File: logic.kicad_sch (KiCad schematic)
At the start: 15 parts, among them U1 SN74ALS08 (КР1533ЛИ1), U11 IN74ALS00N (КР1533ЛА3), U12 IN74ALS02N (КР1533ЛЕ1), U13 SN74ALS10 (КР1533ЛА4), U15 CD4520АN_(К561ИЕ10), U19 SN74ALS04 (КР1533ЛН1), U2 SN74ALS04 (КР1533ЛН1), U3 SN74ALS74AN (КР1533ТМ2), U4 SN74ALS193N_(КР1533ИЕ7), Y1 14 MHz

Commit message: March 21st update
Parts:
- added C3: 220pF, symbol Device:C
- added C32: 82pF, symbol Device:C
- added C8: 120pF, symbol Device:C
- added R15: 510, symbol Device:R
- added R19: 180, symbol Device:R
- added R4, R8: 160, symbol Device:R
- added R5: 10K, symbol Device:R
- added U10: SN74ALS08 (КР1533ЛИ1), Package_DIP:DIP-14_W7.62mm_Socket_LongPads, symbol 74xx:74LS08
- added U14: SN74ALS86N (КР1533ЛП5), Package_DIP:DIP-14_W7.62mm_Socket_LongPads, symbol 74xx:74LS86
- added U17: CD4520АN_(К561ИЕ10), Package_DIP:DIP-16_W7.62mm_Socket_LongPads, symbol w_connectors:CD4520АN_(К561ИЕ10)
- added U18: CD4011 (К561ЛА7), Package_DIP:DIP-14_W7.62mm_Socket_LongPads, symbol 4xx:4011
- added unit 5 of U19
- added unit 3 of U19
- added U20: SN74ALS74AN (КР1533ТМ2), Package_DIP:DIP-14_W7.62mm_Socket_LongPads, symbol 74xx:74LS74
- added U28: IN74ALS32N (КР1533ЛЛ1), Package_DIP:DIP-14_W7.62mm_Socket_LongPads, symbol 74xx:74LS32
- added U49, U7: SN74ALS04 (КР1533ЛН1), Package_DIP:DIP-14_W7.62mm_Socket_LongPads, symbol 74xx:74LS04
- added U5: СD4013АN_(К561ТМ2), Package_DIP:DIP-14_W7.62mm_Socket_LongPads, symbol w_connectors:СD4013АN_(К561ТМ2)
- added U6: CD4015A (К561ИР2), Package_DIP:DIP-16_W7.62mm_Socket_LongPads, symbol 4xxx_IEEE:4015
- added U8, U9: СD4001АN (К561ЛЕ5), Package_DIP:DIP-14_W7.62mm_Socket_LongPads, symbol 4xx:4001
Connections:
- net +5V: now also U15.10 (Enable), U3.10 (~{S}), U3.13 (~{R}), R15.2, U14.10, U20.1 (~{R}), U5.14 (Ucc), U6.16 (Vdd)
- net 7MHZ: now also U11.5, U3.11 (C)
- net GND: now also C3.1, C32.1, C8.1, U17.1 (CK), U17.9 (CK), U5.10 (R2), U5.6 (S1), U5.7 (GND), U5.8 (S2), U6.8 (Vss)
- net UPRMX: now also U19.11
- net at U11.10, U12.5, U4.3 (QA): now also U11.4, U19.5
- net at U11.8, U13.3, U2.1: now also U13.2
- net at U3.5 (Q), U4.5 (UP): now also U20.3 (C)
- net at U1.9, U13.5, U4.6 (QC): now also U14.5
- net at U11.11: now also U1.5
- net at U11.12: now also U11.6
- net ZPRGBD: now reaches U11.13
- net ZPRGBD: now also U3.8 (~{Q})
- net at U3.12 (D): now also U1.13, U13.12
- net BA1: now reaches U15.11 (Q1)
- net BA1: now also U5.11 (C2)
- net BA2: now reaches U15.12 (Q2)
- net BA2: now also R4.1, R5.1
- net BA3: now reaches U15.13 (Q3)
- net BA4: now reaches U15.14 (Q4)
- net BA4: now also U5.4 (R1), U6.7 (D)
- net at U15.15 (Reset): now also U6.6 (MR), U8.10
- net BA0: now reaches U13.4, U15.9 (CK), U4.7 (QD)
- net BA0: now also U14.4
- net at U13.6: now also U10.13
- net at U13.11: now also U13.13, U14.6
- net at U1.4: now also C32.2, R8.2
- net BCASL: now reaches U1.6
- net BRASL: now reaches U1.11
- net at U1.12: now also R8.1, U14.8
- net at U13.1: now also U10.12
- new net: C3.2, R4.2, U7.1
- new net: U18.8, U6.9 (CP), U7.2
- new net: U18.9, U5.1 (Q1), U5.9 (D2)
- new net: U19.10, U28.9
- new net: U10.11, U20.4 (~{S})
- new net: U10.2, U20.5 (Q)
- new net: U7.8, U8.8
- new net: U6.10 (Q4), U7.9, U8.6, U8.9
- new net: U10.3, U49.3
- new net: C8.2, R19.2, U14.9
- new net: R5.2, U5.3 (C1)
- new net: U10.1, U19.6
- new net: U5.5 (D1), U6.3 (Q3), U8.5
- new net: U18.2, U5.12 (Q2o)
- new net BA12: U28.8
- new net BA5: U17.14 (Q4), U17.2 (Enable)
- new net CCML: U17.10 (Enable), U18.10
- new net CT9: U28.10
- new net KGIL: U18.1
- new net KKADRAN: U17.15 (Reset), U17.7 (Reset)
- new net KSGIN: U18.3
- new net OZUMPN: R19.1
- new net VOZUL: U20.2 (D)
- new net Vdd: U6.16 (Vdd)
- new net Vss: U6.8 (Vss)
- new net ТАКТ: R15.1, U49.4
- no-connect marks 2 -> 8
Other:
- note removed: "u10"
- moved on the sheet: C1, C6, R1, R10, R2, U11C, U12B, U13A, U13B, U13C, U15B, U19B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

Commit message: March 22nd additions
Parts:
- added C7: X, symbol Device:C
- added R9, R?: X, symbol Device:R
- added unit 4 of U14
- added unit 6 of U19
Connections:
- net BA0: now also U20.11 (C)
- net BRASL: now also R9.1
- net GND: now also C7.1, U14.13
- net at U20.10 (~{S}): now also U20.13 (~{R})
- net at U20.12 (D): now also U10.12, U10.6, U13.1
- net at U20.9 (Q): now also R?.2
- net at U10.5: now also U8.4
- new net: R?.1, U19.13
- new net: C7.2, R9.2, U14.12
- new net BMX: U14.11
- new net KRAIN: U19.12
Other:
- moved on the sheet: U10B, U18B, U20B, U7B, U7C, U7E, U7F, U9A, U9B, U9C, U9D

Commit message: March 22nd update 2
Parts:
- added C12, C5: Х, symbol Device:C
- added R6: X, symbol Device:R
- added unit 4 of U19
- added U?: SN74ALS257N_(КР1533КП11А), Package_DIP:DIP-16_W7.62mm_Socket_LongPads, symbol w_connectors:SN74ALS257N_(КР1533КП11А)
- gave numbers to parts that had none: 1
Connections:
- net +5V: now also U?.16 (VCC)
- net BA5: now also U6.1 (CP), U9.9
- net CT9: now also U17.5 (Q3), U18.5, U?.13 (I1c), U?.5 (I0b)
- net GND: now also U?.8 (GND)
- net KGIL: now also U9.4
- net KKADRAN: now also U9.11, U19.9
- net UPRMX: now also U?.1 (S)
- net at U7.5: now also U7.4, U8.1, U8.13, U9.13
- net at U7.6: now also R6.2
- net at U7.12: now also U8.2
- net at U7.13: now also U18.4, U6.15 (D)
- net at R13.1, U19.13: now also C12.1
- net at U9.1: now also U6.2 (Q4), U7.3
- net at U9.2: now also U6.13 (Q1)
- net at U9.3: now also U9.5
- net BA6: now reaches U17.3 (Q1)
- net BA7: now reaches U17.4 (Q2)
- net at U17.6 (Q4): now also U18.6
- net at U9.10: now also U18.12, U9.6
- net at U9.8: now also U7.10
- net at U8.11: now also U7.11
- net at U8.12: now also U6.11 (Q3)
- net at U9.12: now also C5.2, R6.1
- net TAIMS: now reaches U18.11
- net CT4: now reaches U18.13
- net CT4: now also U17.13 (Q3), U?.10 (I1d)
- net at U6.14 (MR): now also C12.2, C5.1
- net at U17.11 (Q1): now also U?.6 (I1b)
- net at U17.12 (Q2): now also U?.3 (I1a)
- new net BA10: U?.9 (Zd)
- new net BA11: U?.12 (Zc)
- new net BA8: U?.7 (Zb)
- new net BA9: U?.4 (Za)
- new net ПРL: U19.8
- no-connect marks 8 -> 9
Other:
- moved on the sheet: C32, U10C, U10E, U11A, U11E, U13D, U17A, U17B, U17C, U18B, U18D, U18E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

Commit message: March 22nd - 3rd edition
List 3 is complete
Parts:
- removed C7: X, symbol Device:C
- added C4: 1000pF, symbol Device:C
- C12: value Х -> 120pF
- C5: value Х -> 1000pF
- R13, R9: value X -> 160
- R6: value X -> 10K
- gave numbers to parts that had none: 1
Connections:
- net Vdd is gone; now on net +5V: U6.16 (Vdd)
- net Vss is gone; now on net GND: U6.8 (Vss)
- net +5V: now also U1.14 (VCC), U10.14 (VCC), U11.14 (VCC), U13.14 (VCC), U17.16 (VDD), U18.14 (VDD), U2.14 (VCC), U20.14 (VCC), U28.14 (VCC), U3.14 (VCC), U7.14 (VCC), U8.14 (VDD), U9.14 (VDD)
- net GND: now also C12.2, C5.1, U1.7 (GND), U10.7 (GND), U11.7 (GND), U13.7 (GND), U16.11 (I0d), U16.15 (OE), U17.8 (VSS), U18.7 (VSS), U2.7 (GND), U20.7 (GND), U28.7 (GND), U3.7 (GND), U6.14 (MR), U7.7 (GND), U8.7 (VSS), U9.7 (VSS), C4.1
- net at U8.3: now also U10.4
- net at U7.8, U8.8: now also C4.2
- net at U17.6 (Q4), U18.6: now also U16.2 (I0a)
- no-connect marks 9 -> 31
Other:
- moved on the sheet: C3, U10E, U11E, U13D, U17C, U18E, U19D, U1E, U20C, U28E, U2G, U3C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

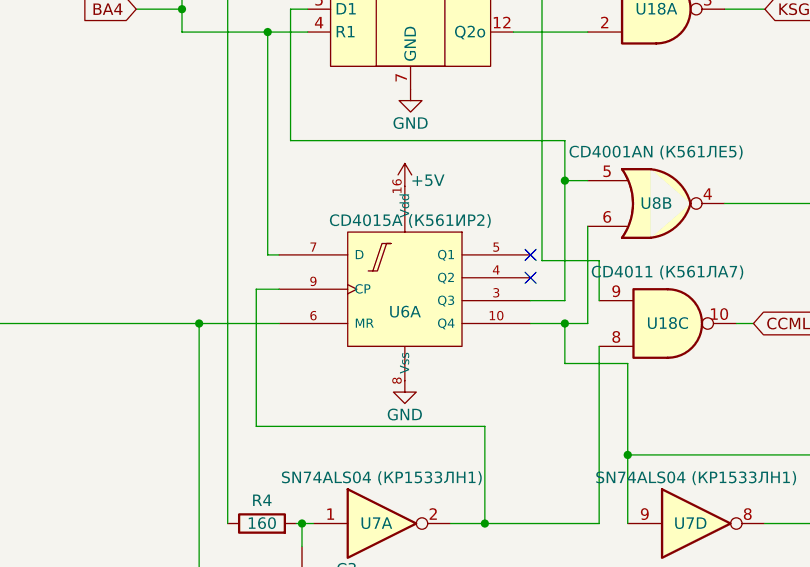
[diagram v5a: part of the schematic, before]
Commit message: March 23rd First pre-alpha
First time ZERO errors and 93 warnings. Schematics are done, now to deal with warnings and footprints.
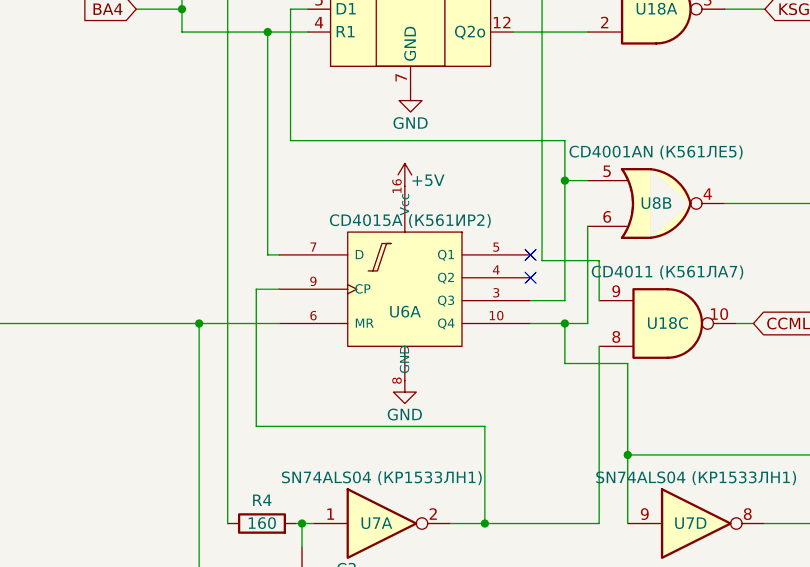
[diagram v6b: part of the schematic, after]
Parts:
- C1, C12, C3, C32, C4, C5, C6, C8: footprint (none) -> Capacitor_THT:C_Disc_D7.0mm_W2.5mm_P5.00mm
- R1, R10, R13, R15, R19, R2, R4, R5, R6, R8, R9: footprint (none) -> Resistor_THT:R_Axial_DIN0207_L6.3mm_D2.5mm_P10.16mm_Horizontal
- U13: footprint (none) -> Package_DIP:DIP-14_W7.62mm_Socket_LongPads
- Y1: footprint (none) -> Crystal:Crystal_HC49-U_Vertical
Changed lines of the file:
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@@
       (effects (font (size 1.27 1.27)) (justify right))
     )
-    (property "Footprint" "" (id 2) (at 77.7748 158.75 0)
+    (property "Footprint" "Capacitor_THT:C_Disc_D7.0mm_W2.5mm_P5.00mm" (id 2) (at 77.7748 158.75 0)
       (effects (font (size 1.27 1.27)) hide)
     )
@@
       (effects (font (size 1.27 1.27)) (justify right))
     )
-    (property "Footprint" "" (id 2) (at 291.7698 227.33 0)
+    (property "Footprint" "Capacitor_THT:C_Disc_D7.0mm_W2.5mm_P5.00mm" (id 2) (at 291.7698 227.33 0)
       (effects (font (size 1.27 1.27)) hide)
     )
@@
     (property "Reference" "R10" (id 0) (at 237.49 42.545 90))
     (property "Value" "330" (id 1) (at 237.49 45.085 90))
-    (property "Footprint" "" (id 2) (at 237.49 48.768 90)
+    (property "Footprint" "Resistor_THT:R_Axial_DIN0207_L6.3mm_D2.5mm_P10.16mm_Horizontal" (id 2) (at 237.49 48.768 90)
       (effects (font (size 1.27 1.27)) hide)
     )
@@
     (property "Reference" "R1" (id 0) (at 86.995 29.21 90))
     (property "Value" "470" (id 1) (at 86.995 31.75 90))
-    (property "Footprint" "" (id 2) (at 86.995 35.433 90)
+    (property "Footprint" "Resistor_THT:R_Axial_DIN0207_L6.3mm_D2.5mm_P10.16mm_Horizontal" (id 2) (at 86.995 35.433 90)
       (effects (font (size 1.27 1.27)) hide)
     )
@@
     (property "Reference" "R13" (id 0) (at 261.62 154.94 90))
     (property "Value" "160" (id 1) (at 264.16 154.94 90))
-    (property "Footprint" "" (id 2) (at 265.938 154.94 90)
+    (property "Footprint" "Resistor_THT:R_Axial_DIN0207_L6.3mm_D2.5mm_P10.16mm_Horizontal" (id 2) (at 265.938 154.94 90)
       (effects (font (size 1.27 1.27)) hide)
     )
@@
     (property "Reference" "Y1" (id 0) (at 67.31 47.625 0))
     (property "Value" "14 MHz" (id 1) (at 67.31 50.165 0))
-    (property "Footprint" "" (id 2) (at 67.31 55.245 0)
+    (property "Footprint" "Crystal:Crystal_HC49-U_Vertical" (id 2) (at 67.31 55.245 0)
       (effects (font (size 1.27 1.27)) hide)
     )
@@
       (effects (font (size 1.27 1.27)) (justify right))
     )
-    (property "Footprint" "" (id 2) (at 162.2298 123.825 0)
+    (property "Footprint" "Capacitor_THT:C_Disc_D7.0mm_W2.5mm_P5.00mm" (id 2) (at 162.2298 123.825 0)
       (effects (font (size 1.27 1.27)) hide)
     )
@@
     (property "Reference" "R4" (id 0) (at 74.295 153.67 90))
     (property "Value" "160" (id 1) (at 74.295 156.21 90))
-    (property "Footprint" "" (id 2) (at 74.295 157.988 90)
+    (property "Footprint" "Resistor_THT:R_Axial_DIN0207_L6.3mm_D2.5mm_P10.16mm_Horizontal" (id 2) (at 74.295 157.988 90)
       (effects (font (size 1.27 1.27)) hide)
     )
@@
     (property "Reference" "R5" (id 0) (at 73.66 93.98 90))
     (property "Value" "10K" (id 1) (at 75.565 96.52 90))
-    (property "Footprint" "" (id 2) (at 75.565 98.298 90)
+    (property "Footprint" "Resistor_THT:R_Axial_DIN0207_L6.3mm_D2.5mm_P10.16mm_Horizontal" (id 2) (at 75.565 98.298 90)
       (effects (font (size 1.27 1.27)) hide)
     )
@@
       (effects (font (size 1.27 1.27)) (justify right))
     )
-    (property "Footprint" "" (id 2) (at 324.993 86.995 90)
+    (property "Footprint" "Resistor_THT:R_Axial_DIN0207_L6.3mm_D2.5mm_P10.16mm_Horizontal" (id 2) (at 324.993 86.995 90)
       (effects (font (size 1.27 1.27)) hide)
     )
@@
     (property "Reference" "R19" (id 0) (at 156.21 121.285 90))
     (property "Value" "180" (id 1) (at 156.21 123.825 90))
-    (property "Footprint" "" (id 2) (at 156.21 125.603 90)
+    (property "Footprint" "Resistor_THT:R_Axial_DIN0207_L6.3mm_D2.5mm_P10.16mm_Horizontal" (id 2) (at 156.21 125.603 90)
       (effects (font (size 1.27 1.27)) hide)
     )
@@
     (property "Reference" "R8" (id 0) (at 203.2 113.665 90))
     (property "Value" "160" (id 1) (at 203.2 116.205 90))
-    (property "Footprint" "" (id 2) (at 203.2 117.983 90)
+    (property "Footprint" "Resistor_THT:R_Axial_DIN0207_L6.3mm_D2.5mm_P10.16mm_Horizontal" (id 2) (at 203.2 117.983 90)
       (effects (font (size 1.27 1.27)) hide)
     )
@@
       (effects (font (size 1.27 1.27)) (justify right))
     )
-    (property "Footprint" "" (id 2) (at 209.2198 117.475 0)
+    (property "Footprint" "Capacitor_THT:C_Disc_D7.0mm_W2.5mm_P5.00mm" (id 2) (at 209.2198 117.475 0)
       (effects (font (size 1.27 1.27)) hide)
     )
@@
     (property "Reference" "R9" (id 0) (at 281.305 136.525 90))
     (property "Value" "160" (id 1) (at 281.305 139.065 90))
-    (property "Footprint" "" (id 2) (at 281.305 140.843 90)
+    (property "Footprint" "Resistor_THT:R_Axial_DIN0207_L6.3mm_D2.5mm_P10.16mm_Horizontal" (id 2) (at 281.305 140.843 90)
       (effects (font (size 1.27 1.27)) hide)
     )
@@
     (property "Reference" "R6" (id 0) (at 290.195 194.31 90))
     (property "Value" "10K" (id 1) (at 292.735 194.31 90))
-    (property "Footprint" "" (id 2) (at 294.513 194.31 90)
+    (property "Footprint" "Resistor_THT:R_Axial_DIN0207_L6.3mm_D2.5mm_P10.16mm_Horizontal" (id 2) (at 294.513 194.31 90)
       (effects (font (size 1.27 1.27)) hide)
     )
@@
       (effects (font (size 1.27 1.27)) (justify right))
     )
-    (property "Footprint" "" (id 2) (at 254.635 164.1602 0)
+    (property "Footprint" "Capacitor_THT:C_Disc_D7.0mm_W2.5mm_P5.00mm" (id 2) (at 254.635 164.1602 0)
       (effects (font (size 1.27 1.27)) hide)
     )
@@
     (property "Reference" "U13" (id 0) (at 177.165 66.04 0))
     (property "Value" "SN74ALS10 (КР1533ЛА4)" (id 1) (at 177.8 60.96 0))
-    (property "Footprint" "" (id 2) (at 177.165 66.04 0)
+    (property "Footprint" "Package_DIP:DIP-14_W7.62mm_Socket_LongPads" (id 2) (at 177.165 66.04 0)
       (effects (font (size 1.27 1.27)) hide)
     )
@@
       (effects (font (size 1.27 1.27)) (justify right))
     )
-    (property "Footprint" "" (id 2) (at 244.7798 46.99 0)
+    (property "Footprint" "Capacitor_THT:C_Disc_D7.0mm_W2.5mm_P5.00mm" (id 2) (at 244.7798 46.99 0)
       (effects (font (size 1.27 1.27)) hide)
     )
@@
     (property "Reference" "U13" (id 0) (at 222.25 36.83 0))
     (property "Value" "SN74ALS10 (КР1533ЛА4)" (id 1) (at 222.25 31.115 0))
-    (property "Footprint" "" (id 2) (at 222.25 36.83 0)
+    (property "Footprint" "Package_DIP:DIP-14_W7.62mm_Socket_LongPads" (id 2) (at 222.25 36.83 0)
       (effects (font (size 1.27 1.27)) hide)
     )
@@
     (property "Reference" "C1" (id 0) (at 68.58 36.83 90))
     (property "Value" "120pF" (id 1) (at 68.58 39.37 90))
-    (property "Footprint" "" (id 2) (at 72.39 42.2148 0)
+    (property "Footprint" "Capacitor_THT:C_Disc_D7.0mm_W2.5mm_P5.00mm" (id 2) (at 72.39 42.2148 0)
       (effects (font (size 1.27 1.27)) hide)
     )
@@
       (effects (font (size 1.27 1.27)) (justify right))
     )
-    (property "Footprint" "" (id 2) (at 135.5598 159.385 0)
+    (property "Footprint" "Capacitor_THT:C_Disc_D7.0mm_W2.5mm_P5.00mm" (id 2) (at 135.5598 159.385 0)
       (effects (font (size 1.27 1.27)) hide)
     )
@@
       (effects (font (size 1.27 1.27)) (justify left))
     )
-    (property "Footprint" "" (id 2) (at 220.98 -167.64 0)
+    (property "Footprint" "Package_DIP:DIP-14_W7.62mm_Socket_LongPads" (id 2) (at 220.98 -167.64 0)
       (effects (font (size 1.27 1.27)) hide)
     )
@@
     (property "Reference" "U13" (id 0) (at 223.52 69.215 0))
     (property "Value" "SN74ALS10 (КР1533ЛА4)" (id 1) (at 223.52 63.5 0))
-    (property "Footprint" "" (id 2) (at 223.52 69.215 0)
+    (property "Footprint" "Package_DIP:DIP-14_W7.62mm_Socket_LongPads" (id 2) (at 223.52 69.215 0)
       (effects (font (size 1.27 1.27)) hide)
     )
@@
     (property "Reference" "R2" (id 0) (at 51.435 28.575 90))
     (property "Value" "430" (id 1) (at 51.435 31.115 90))
-    (property "Footprint" "" (id 2) (at 51.435 34.798 90)
-      (effects (font (size 1.27 1.27)) hide)
-    )
+    (property "Footprint" "Resistor_THT:R_Axial_DIN0207_L6.3mm_D2.5mm_P10.16mm_Horizontal" (id 2) (at 51.435 34.798 90)
+      (effects (font (size 1.27 1.27)) hide)
+    )

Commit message: March 26th update
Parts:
- U1, U10, U11, U12, U13, U14, U18, U19, U2, U20, U28, U3, U49, U5, U7, U8, U9: footprint Package_DIP:DIP-14_W7.62mm_Socket_LongPads -> Package_DIP:DIP-14_W7.62mm_Socket
- U15, U16, U17, U4, U6: footprint Package_DIP:DIP-16_W7.62mm_Socket_LongPads -> Package_DIP:DIP-16_W7.62mm_Socket
